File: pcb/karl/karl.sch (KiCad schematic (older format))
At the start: 30 parts, among them J1 Raspberry_Pi, J2 Power, J3 Battery, J4 Motor Power, J5 LIDAR_Power, Q1 MMBT3904, Q2 MMBT3904, U1 MCP3421A0T-ECH

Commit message: added pwm an motor module
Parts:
- removed J4: Motor Power, TerminalBlock:TerminalBlock_bornier-2_P5.08mm, symbol Connector:Screw_Terminal_01x02
- added J6, J7: Power, TerminalBlock:TerminalBlock_bornier-2_P5.08mm, symbol Connector:Screw_Terminal_01x02
- added U?: DRV8848, Package_SO:TSSOP-16-1EP_4.4x5mm_P0.65mm, symbol Driver_Motor:DRV8848
- added U?: PCA9685PW, Package_SO:TSSOP-28_4.4x9.7mm_P0.65mm, symbol Driver_LED:PCA9685PW
- J3: footprint TerminalBlock:TerminalBlock_bornier-2_P5.08mm -> Connector_PinHeader_2.54mm:PinHeader_1x02_P2.54mm_Vertical; symbol Connector:Screw_Terminal_01x02 -> Connector:Conn_01x02_Male
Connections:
- net +5V: now also U?.1 (nSLEEP), U?.11 (VREF), U?.12 (VM), U?.14 (VINT), U?.28 (VDD)
- net +BATT: now also J3.1 (Pin_1); no longer J3.2 (Pin_2)
- net GND: now also U?.13 (GND), U?.14 (VSS), U?.17 (PPAD), U?.3 (AISEN), U?.6 (BISEN)
- net GNDA: now also J3.2 (Pin_2); no longer J3.1 (Pin_1)
- net GPIO_23: no longer R3.2
- net GPIO_24: no longer R4.2
- net SCL: now also U?.26 (SCL)
- net SDA: now also U?.27 (SDA)
- new net: J6.1 (Pin_1), U?.2 (AOUT1)
- new net: J6.2 (Pin_2), U?.4 (AOUT2)
- new net: J7.2 (Pin_2), U?.5 (BOUT2)
- new net: J7.1 (Pin_1), U?.7 (BOUT1)
- new net PWM_00: U?.16 (AIN1), U?.6 (LED0)
- new net PWM_01: U?.15 (AIN2), U?.7 (LED1)
- new net PWM_02: U?.8 (LED2), U?.9 (BIN1)
- new net PWM_03: U?.10 (BIN2), U?.9 (LED3)
- new net PWM_04: R3.2, U?.10 (LED4)
- new net PWM_05: R4.2, U?.11 (LED5)
- new net PWM_06: U?.12 (LED6)
- new net PWM_07: U?.13 (LED7)
- new net PWM_08: U?.15 (LED8)
- new net PWM_09: U?.16 (LED9)
- new net PWM_10: U?.17 (LED10)
- new net PWM_11: U?.18 (LED11)
- new net PWM_12: U?.19 (LED12)
- new net PWM_13: U?.20 (LED13)
- new net PWM_14: U?.21 (LED14)
- new net PWM_15: U?.22 (LED15)
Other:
- note added: "AIN1\n\nAIN2\n\nBIN1\n\nBIN2\n\nL LIGHT\n\nR LIGHT"
- note added: "Motor Driver"
- note added: "PWM Module"
- note removed: "Motor Power"

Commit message: added Pi Hat layout and OLED display
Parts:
- added J4: OLED, Connector_PinHeader_2.54mm:PinHeader_1x04_P2.54mm_Vertical, symbol Connector:Conn_01x04_Female
- J6: value Power -> Motor A
- J7: value Power -> Motor B
- gave numbers to parts that had none: 2
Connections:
- net +3V3: now also J4.2 (Pin_2)
- net GND: now also J4.1 (Pin_1)
- net SCL: now also J4.3 (Pin_3)
- net SDA: now also J4.4 (Pin_4)
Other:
- note added: "OLED Display"
- moved on the sheet: J5, J6, J7, U3

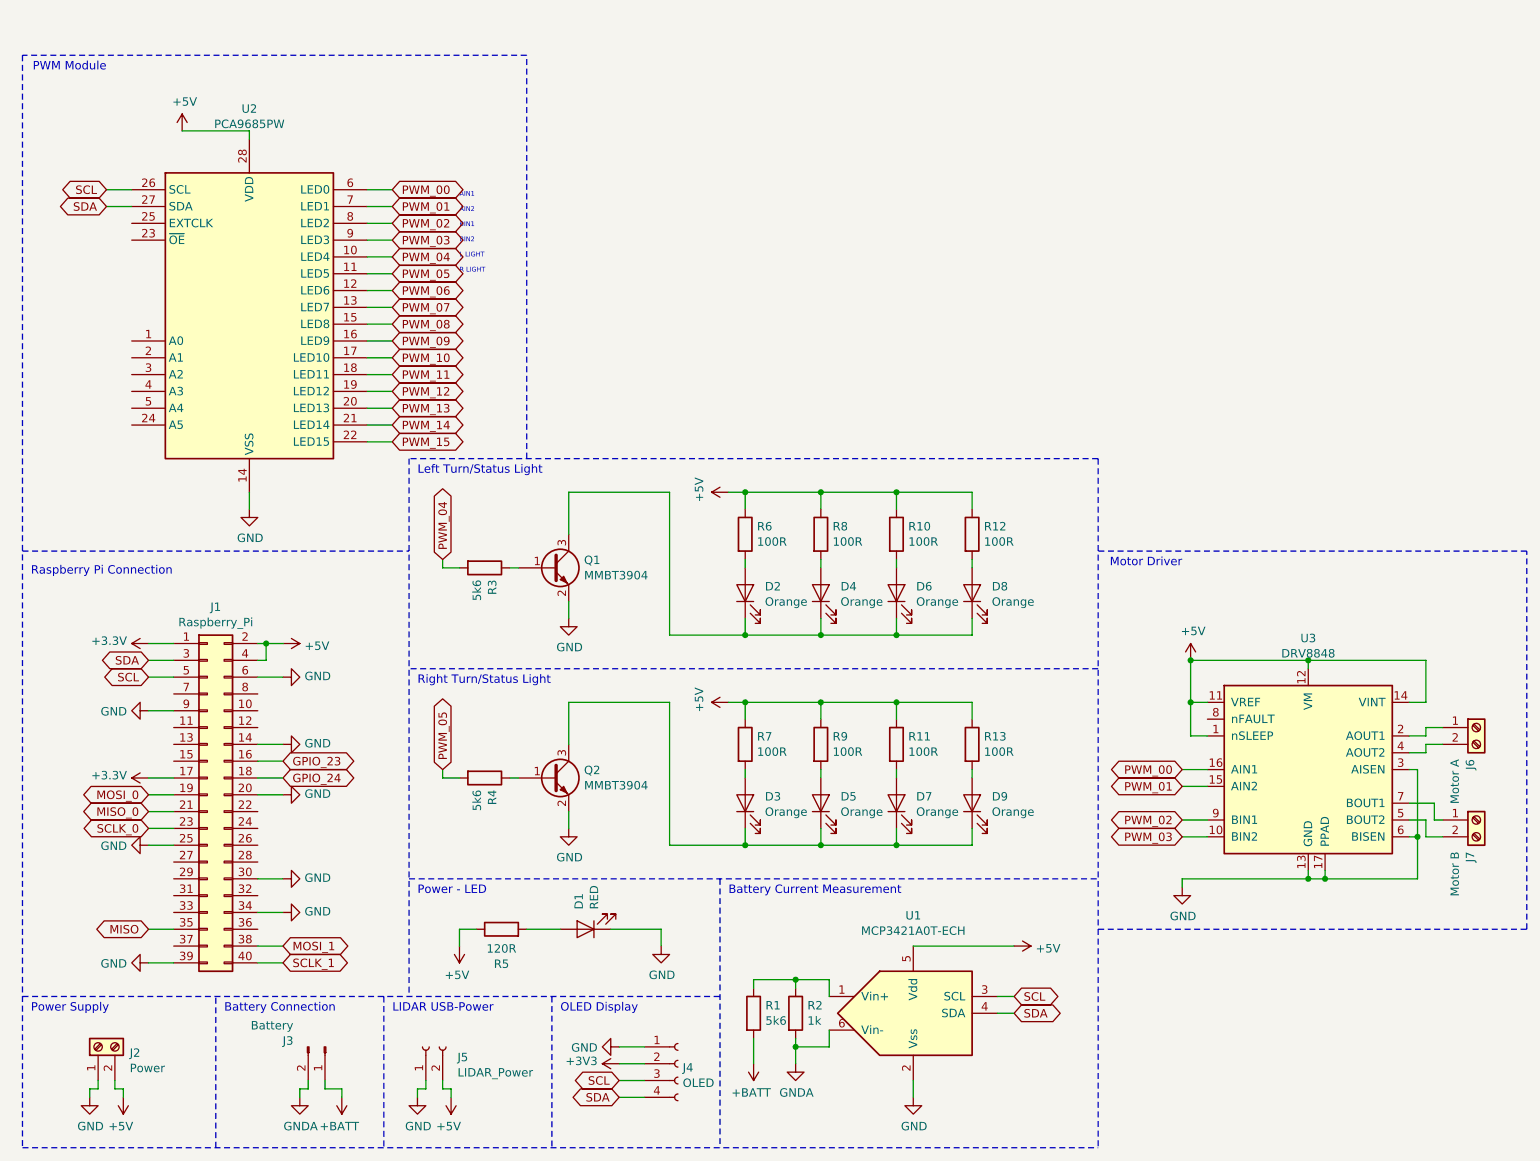
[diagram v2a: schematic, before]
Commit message: added MPU6050
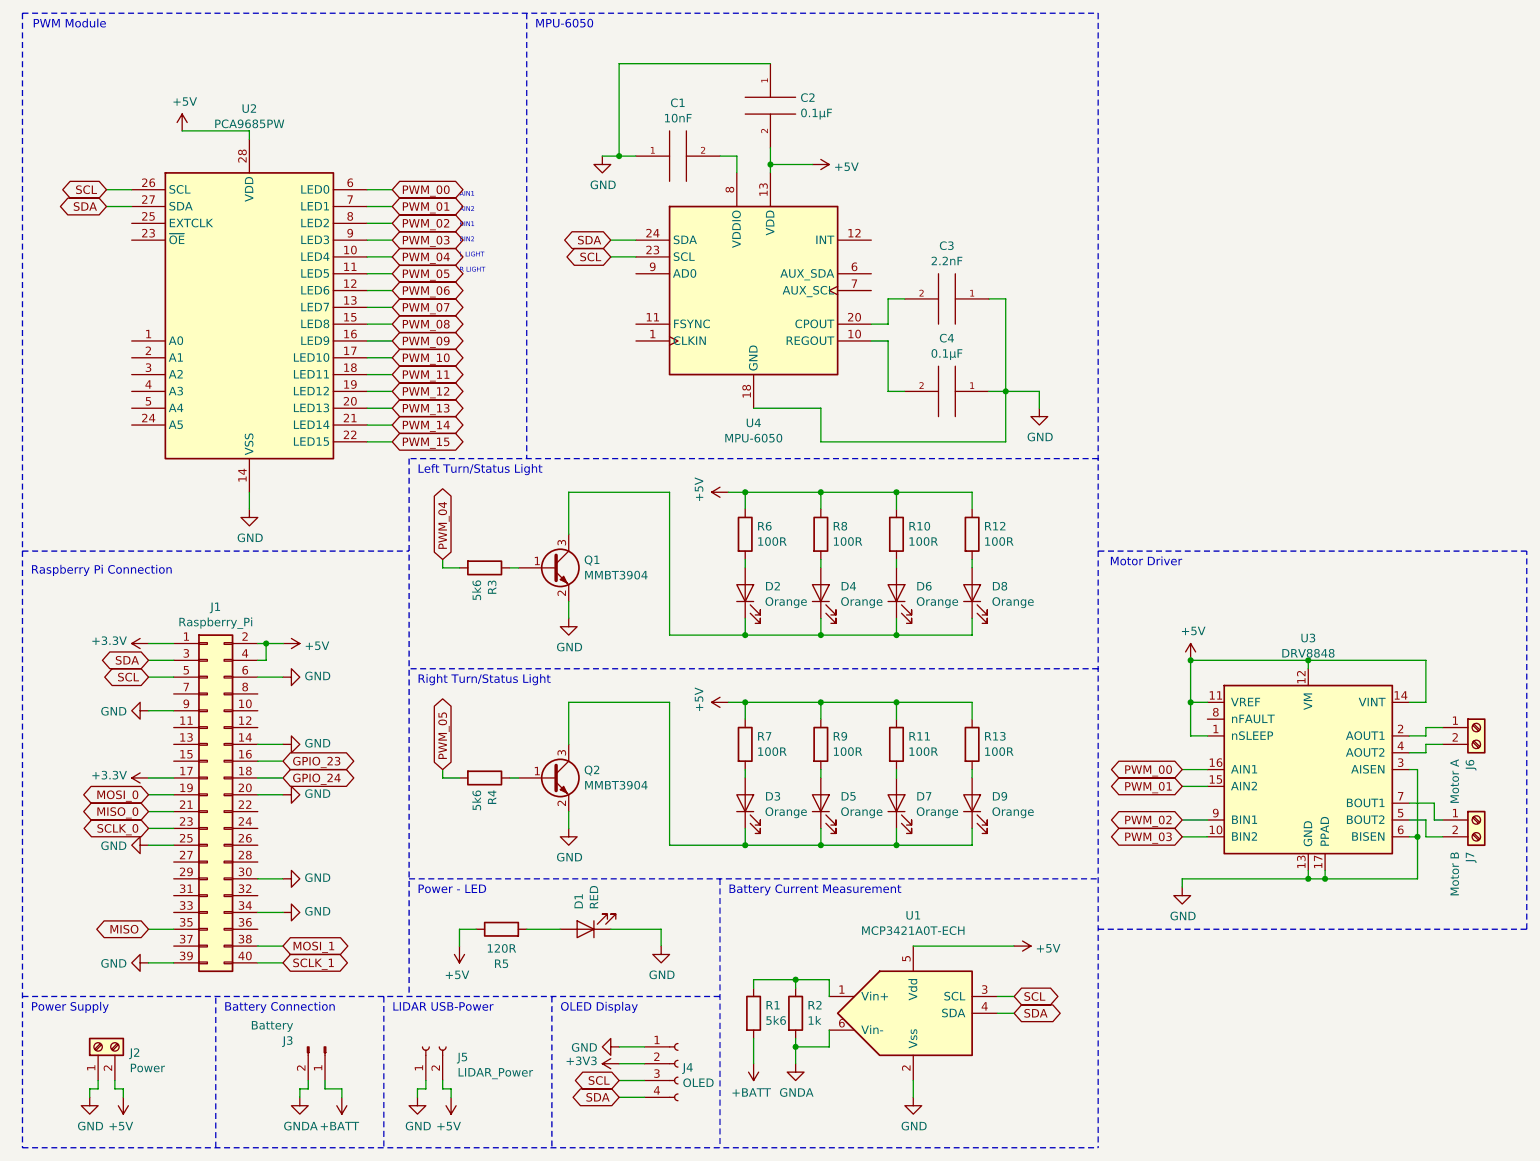
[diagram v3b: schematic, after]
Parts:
- added C1: 10nF, Capacitor_SMD:C_0201_0603Metric, symbol pspice:C
- added C2, C4: 0.1µF, Capacitor_SMD:C_0201_0603Metric, symbol pspice:C
- added C3: 2.2nF, Capacitor_SMD:C_0201_0603Metric, symbol pspice:C
- added U4: MPU-6050, Sensor_Motion:InvenSense_QFN-24_4x4mm_P0.5mm, symbol Sensor_Motion:MPU-6050
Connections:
- net +5V: now also C2.2, U4.13 (VDD)
- net GND: now also C1.1, C2.1, C3.1, C4.1, U4.18 (GND)
- net SCL: now also U4.23 (SCL)
- net SDA: now also U4.24 (SDA)
- new net: C4.2, U4.10 (REGOUT)
- new net: C3.2, U4.20 (CPOUT)
- new net: C1.2, U4.8 (VDDIO)
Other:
- note added: "MPU-6050"
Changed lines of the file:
@@
 	1    0    0    -1
 $EndComp
-Wire Notes Line
-	3500 3650 3500 1250
-Wire Notes Line
-	3500 1250 500  1250
-Wire Notes Line
-	500  1250 500  7750
 Text GLabel 1000 2050 0    50   BiDi ~ 0
 SCL
@@
 Wire Wire Line
 	1850 3950 1850 3850
-Text Notes 1000 1350 2    50   ~ 0
+Text Notes 1000 1100 2    50   ~ 0
 PWM Module
 $Comp
@@
 AIN1\n\nAIN2\n\nBIN1\n\nBIN2\n\nL LIGHT\n\nR LIGHT
 Wire Notes Line
-	6900 3650 6900 7750
-Wire Notes Line
 	6900 6450 9450 6450
 Wire Notes Line
@@
 Wire Wire Line
 	4200 7150 4050 7150
+$Comp
+L Sensor_Motion:MPU-6050 U4
+U 1 1 5E731C73
+P 4850 2650
+F 0 "U4" H 4850 1861 50  0000 C CNN
+F 1 "MPU-6050" H 4850 1770 50  0000 C CNN
+F 2 "Sensor_Motion:InvenSense_QFN-24_4x4mm_P0.5mm" H 4850 1850 50  0001 C CNN
+F 3 "https://store.invensense.com/datasheets/invensense/MPU-6050_DataSheet_V3%204.pdf" H 4850 2500 50  0001 C CNN
+F 4 "C24112" H 4850 2650 50  0001 C CNN "LCSC"
+	1    4850 2650
+	1    0    0    -1
+$EndComp
+Text GLabel 4000 2350 0    50   BiDi ~ 0
+SDA
+Text GLabel 4000 2450 0    50   BiDi ~ 0
+SCL
+$Comp
+L power:GND #PWR0134
+U 1 1 5E745F9E
+P 6550 3350
+F 0 "#PWR0134" H 6550 3100 50  0001 C CNN
+F 1 "GND" H 6555 3177 50  0000 C CNN
+F 2 "" H 6550 3350 50  0001 C CNN
+F 3 "" H 6550 3350 50  0001 C CNN
+	1    6550 3350
+	1    0    0    -1
+$EndComp
+$Comp
+L pspice:C C2
+U 1 1 5E759335
+P 4950 1550
+F 0 "C2" H 5128 1596 50  0000 L CNN
+F 1 "0.1µF" H 5128 1505 50  0000 L CNN
+F 2 "Capacitor_SMD:C_0201_0603Metric" H 4950 1550 50  0001 C CNN
+F 3 "~" H 4950 1550 50  0001 C CNN
+	1    4950 1550
+	1    0    0    -1
+$EndComp
+$Comp
+L pspice:C C4
+U 1 1 5E759ED2
+P 6000 3250
+F 0 "C4" V 5685 3250 50  0000 C CNN
+F 1 "0.1µF" V 5776 3250 50  0000 C CNN
+F 2 "Capacitor_SMD:C_0201_0603Metric" H 6000 3250 50  0001 C CNN
+F 3 "~" H 6000 3250 50  0001 C CNN
+	1    6000 3250
+	0    1    1    0
+$EndComp
+$Comp
+L pspice:C C3
+U 1 1 5E793D6D
+P 6000 2700
+F 0 "C3" V 5685 2700 50  0000 C CNN
+F 1 "2.2nF" V 5776 2700 50  0000 C CNN
+F 2 "Capacitor_SMD:C_0201_0603Metric" H 6000 2700 50  0001 C CNN
+F 3 "~" H 6000 2700 50  0001 C CNN
+	1    6000 2700
+	0    1    1    0
+$EndComp
+$Comp
+L pspice:C C1
+U 1 1 5E794685
+P 4400 1850
+F 0 "C1" V 4715 1850 50  0000 C CNN
+F 1 "10nF" V 4624 1850 50  0000 C CNN
+F 2 "Capacitor_SMD:C_0201_0603Metric" H 4400 1850 50  0001 C CNN
+F 3 "~" H 4400 1850 50  0001 C CNN
+	1    4400 1850
+	0    -1   -1   0
+$EndComp
+Wire Wire Line
+	4750 1950 4750 1850
+Wire Wire Line
+	4750 1850 4650 1850
+Wire Wire Line
+	4150 2350 4000 2350
+Wire Wire Line
+	4000 2450 4150 2450
+Wire Wire Line
+	5750 2700 5650 2700
+Wire Wire Line
+	5650 2700 5650 2850
+Wire Wire Line
+	5650 2850 5550 2850
+Wire Wire Line
+	6350 2700 6250 2700
+Wire Wire Line
+	6250 3250 6350 3250
+Wire Wire Line
+	6350 3250 6350 2700
+Wire Wire Line
+	5750 3250 5650 3250
+Wire Wire Line
+	5650 3250 5650 2950
+Wire Wire Line
+	5650 2950 5550 2950
+Wire Wire Line
+	4950 1800 4950 1900
+Wire Wire Line
+	4950 1300 4050 1300
+Wire Wire Line
+	4050 1300 4050 1850
+Wire Wire Line
+	4050 1850 4150 1850
+$Comp
+L power:GND #PWR0135
+U 1 1 5E848F67
+P 3950 1850
+F 0 "#PWR0135" H 3950 1600 50  0001 C CNN
+F 1 "GND" H 3955 1677 50  0000 C CNN
+F 2 "" H 3950 1850 50  0001 C CNN
+F 3 "" H 3950 1850 50  0001 C CNN
+	1    3950 1850
+	1    0    0    -1
+$EndComp
+Wire Wire Line
+	3950 1850 4050 1850
+Connection ~ 4050 1850
+$Comp
+L power:+5V #PWR0136
+U 1 1 5E853D3C
+P 5200 1900
+F 0 "#PWR0136" H 5200 1750 50  0001 C CNN
+F 1 "+5V" V 5215 2028 50  0000 L CNN
+F 2 "" H 5200 1900 50  0001 C CNN
+F 3 "" H 5200 1900 50  0001 C CNN
+	1    5200 1900
+	0    1    1    0
+$EndComp
+Wire Wire Line
+	5200 1900 4950 1900
+Connection ~ 4950 1900
+Wire Wire Line
+	4950 1900 4950 1950
+Wire Wire Line
+	6350 3250 6550 3250
+Wire Wire Line
+	6550 3250 6550 3350
+Connection ~ 6350 3250
+Wire Wire Line
+	6350 3250 6350 3550
+Wire Wire Line
+	6350 3550 5250 3550
+Wire Wire Line
+	5250 3550 5250 3350
+Wire Wire Line
+	5250 3350 4850 3350
+Wire Notes Line
+	3500 1000 3500 3650
+Wire Notes Line
+	500  1000 500  7750
+Wire Notes Line
+	6900 1000 6900 7750
+Wire Notes Line
+	500  1000 6900 1000
+Text Notes 3550 1100 0    50   ~ 0
+MPU-6050
 $EndSCHEMATC
